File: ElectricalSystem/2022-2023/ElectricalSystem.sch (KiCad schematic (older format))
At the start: 33 parts

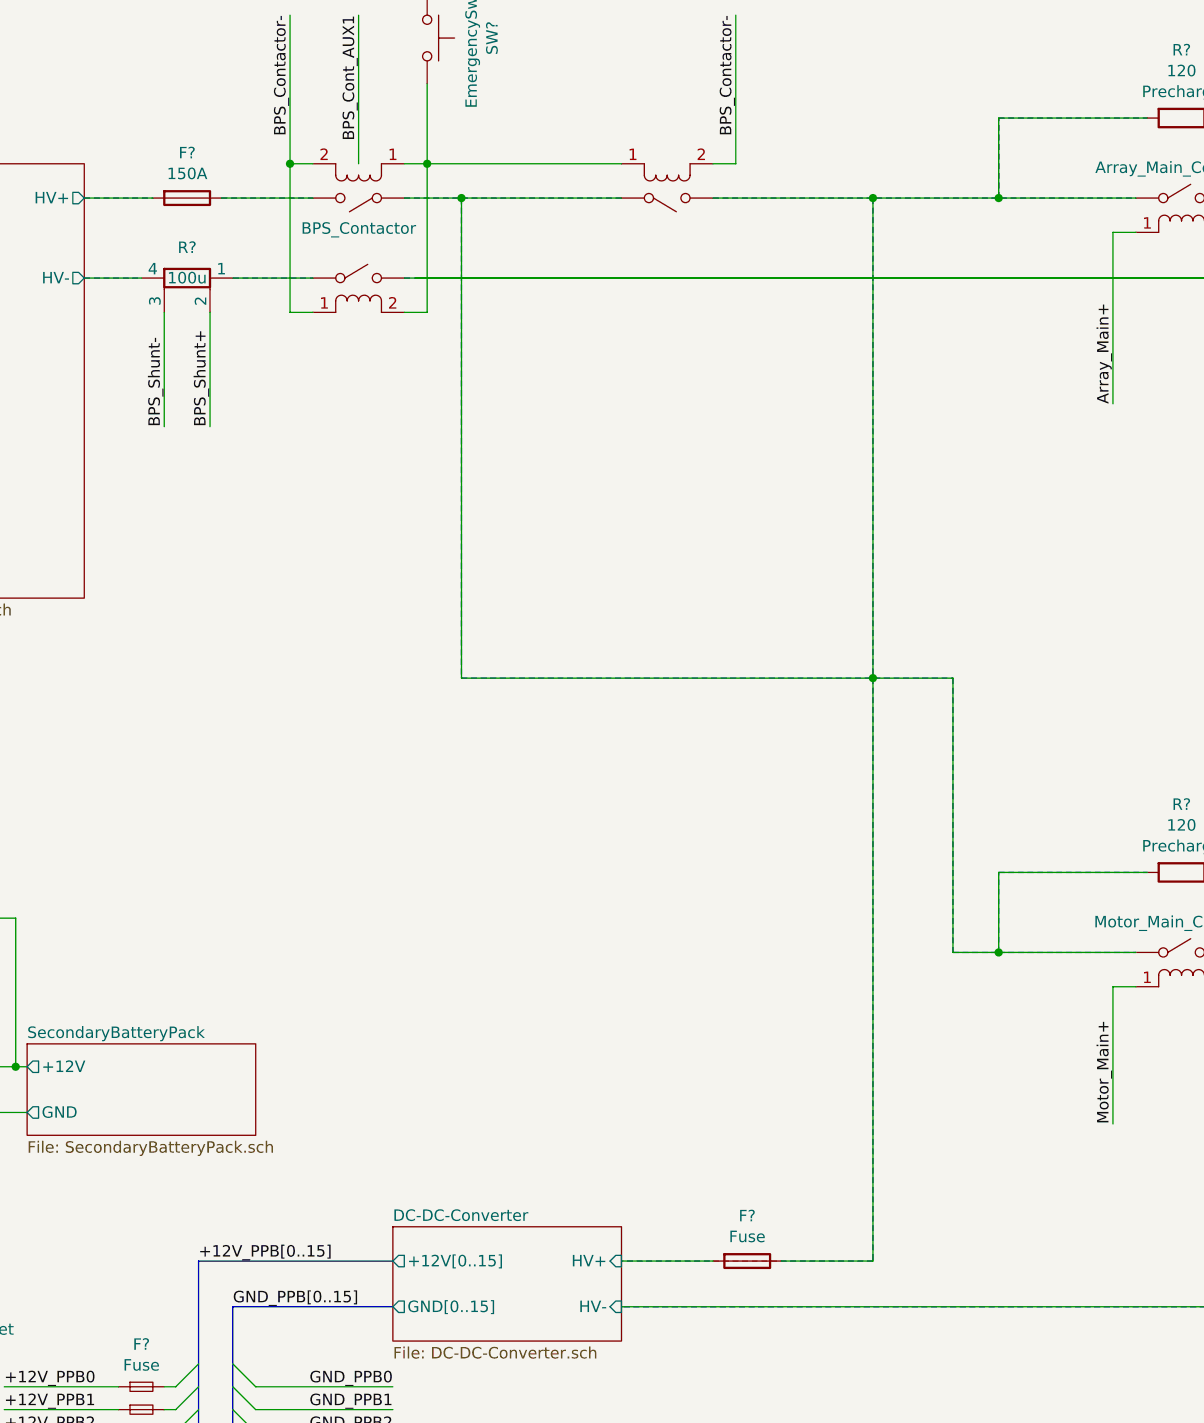
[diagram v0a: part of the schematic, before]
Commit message: Adds updated electrical system for 2022-2023
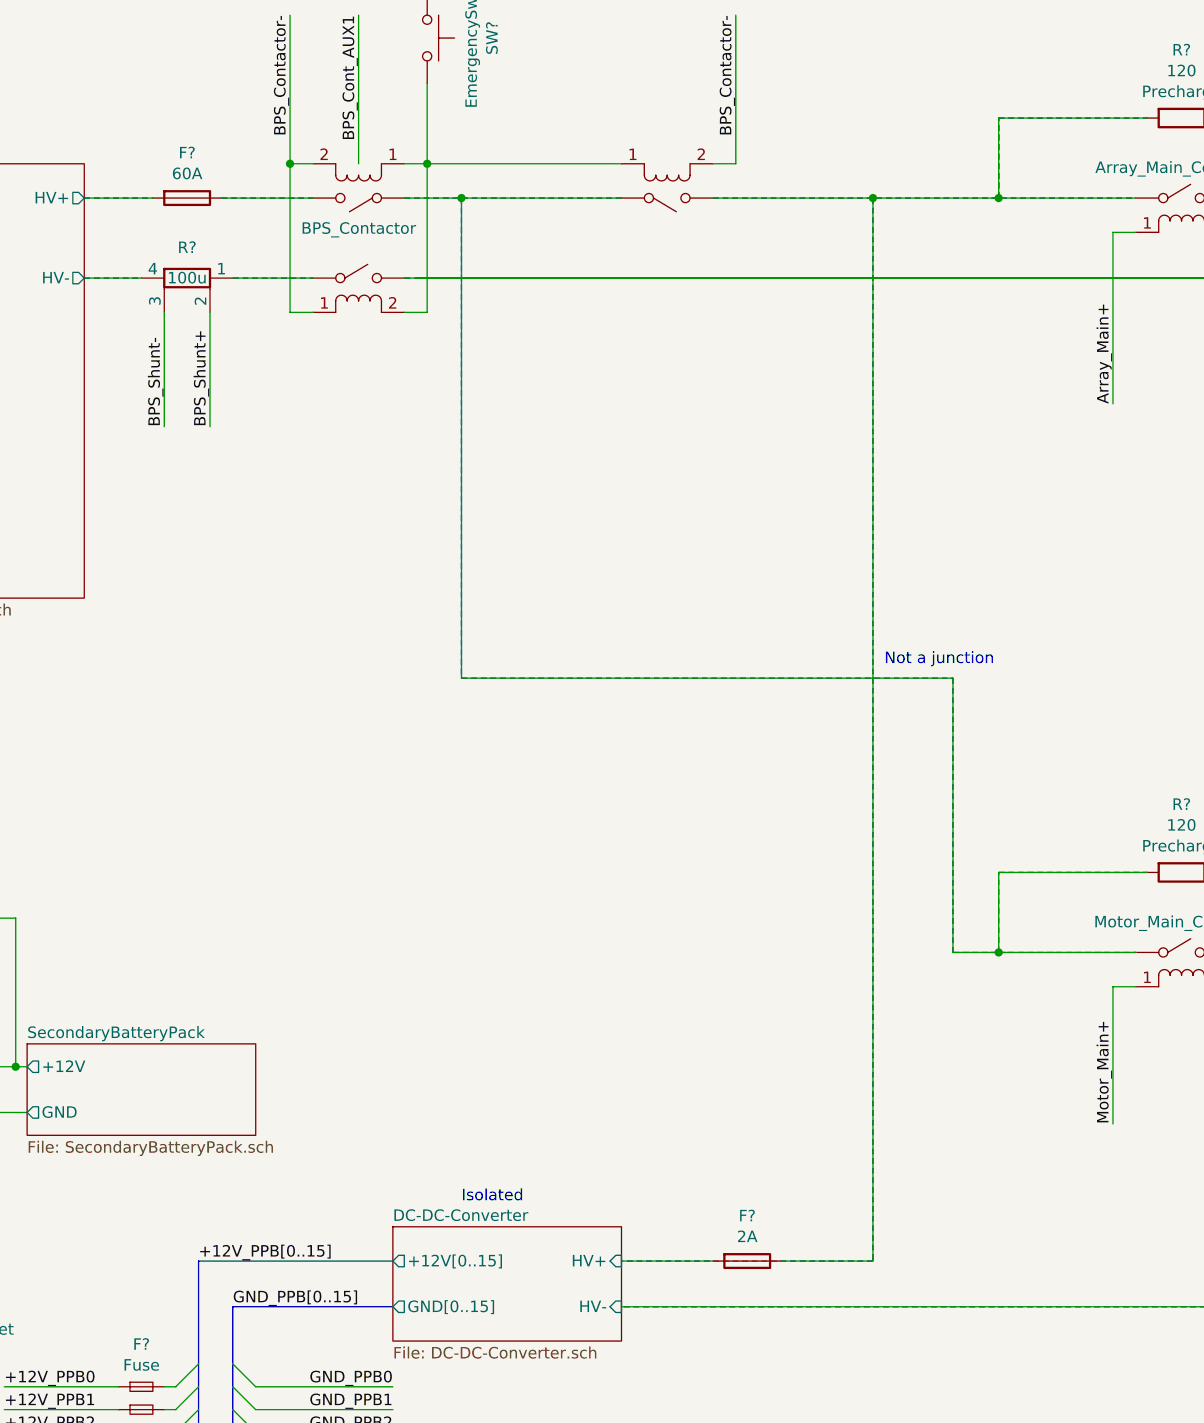
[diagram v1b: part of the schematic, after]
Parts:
- F?: value 150A -> 60A
- F?: value Fuse -> 2A
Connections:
- new net: F?.1, R?.2, U?.~, U?.~
- new net: R?.2, U?.~, U?.~, U?.~
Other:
- note added: "Isolated"
- note added: "Not a junction"
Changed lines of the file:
@@
 $Descr B 17000 11000
 encoding utf-8
-Sheet 1 16
+Sheet 1 17
 Title ""
 Date ""
@@
 P 7500 2350
 F 0 "F?" V 7303 2350 50  0000 C CNN
-F 1 "150A" V 7394 2350 50  0000 C CNN
+F 1 "60A" V 7394 2350 50  0000 C CNN
 F 2 "" V 7430 2350 50  0001 C CNN
 F 3 "~" H 7500 2350 50  0001 C CNN
@@
 Wire Wire Line
 	9400 7200 12600 7200
-Wire Notes Line width 20 style solid rgb(255, 0, 0)
-	10500 2350 10500 7000
 Wire Notes Line width 20 style solid rgb(255, 0, 0)
 	10500 7000 9400 7000
@@
 $EndComp
 Wire Wire Line
-	8700 4450 10500 4450
-Wire Wire Line
 	10850 4450 10850 5650
 Wire Wire Line
@@
 Text Notes 6700 9250 0    50   ~ 0
 Fuses located within\na fuse box
-Wire Wire Line
-	9800 2350 10500 2350
 Wire Wire Line
 	9900 2200 9800 2200
@@
 P 9950 7000
 F 0 "F?" V 9753 7000 50  0000 C CNN
-F 1 "Fuse" V 9844 7000 50  0000 C CNN
+F 1 "2A" V 9844 7000 50  0000 C CNN
 F 2 "" V 9880 7000 50  0001 C CNN
 F 3 "~" H 9950 7000 50  0001 C CNN
@@
 Wire Wire Line
 	10100 7000 10500 7000
-Wire Wire Line
-	10500 7000 10500 4450
-Connection ~ 10500 4450
-Wire Wire Line
-	10500 4450 10850 4450
-Wire Wire Line
-	10500 4450 10500 2350
-Connection ~ 10500 2350
-Wire Wire Line
-	10500 2350 11050 2350
 Wire Wire Line
 	8700 4450 8700 2350
@@
 Wire Wire Line
 	6750 5500 6750 6150
+Wire Wire Line
+	9800 2350 10500 2350
+Wire Notes Line width 20 style solid rgb(255, 0, 0)
+	10500 2350 10500 7000
+Wire Wire Line
+	8700 4450 10850 4450
+Wire Wire Line
+	10500 2350 10500 7000
 Wire Bus Line
 	7700 7200 7700 9150
 Wire Bus Line
 	7550 7000 7550 9150
+Connection ~ 10500 2350
+Wire Wire Line
+	10500 2350 11050 2350
+Text Notes 10550 4400 0    50   ~ 0
+Not a junction
+Text Notes 8700 6750 0    50   ~ 0
+Isolated
 $EndSCHEMATC
